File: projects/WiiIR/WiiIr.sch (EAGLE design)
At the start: 20 parts

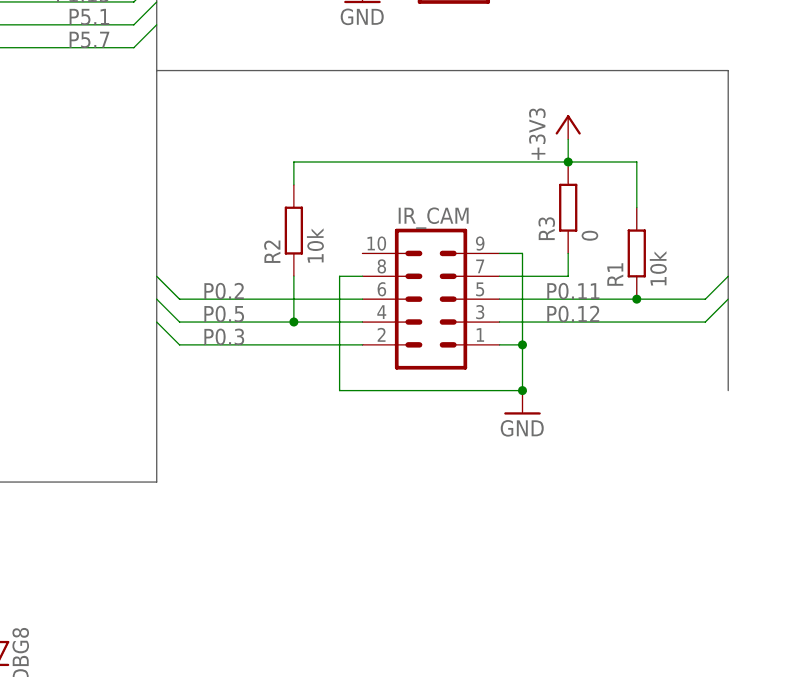
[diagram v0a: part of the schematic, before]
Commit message: Restructured + PCB v1 issues solved
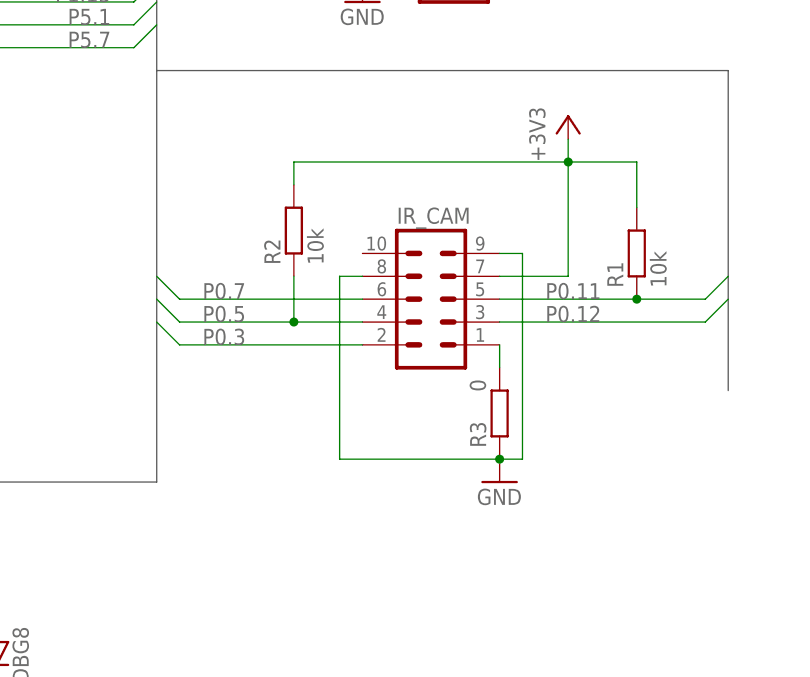
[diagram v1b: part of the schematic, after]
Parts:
- C2: device resistor:C-EU050-024X044 -> resistor:C-EU025-025X050
- R1: device resistor:R-EU_0207/10 -> resistor:R-EU_0207/15
- R3: device resistor:R-EU_0207/12 -> resistor:R-EU_0207/10
- SV1, SV2: device con-lstb:MA20-2 -> con-lstb:MA20-2BIG
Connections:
- removed net N$1: IR_CAM.7, R3.1
- new net N$12: IR_CAM.1, R3.1
- net +3V3: now also IR_CAM.7; no longer R3.2
- net GND: now also R3.2; no longer IR_CAM.1
- net P0.2: no longer IR_CAM.6
- net P0.7: now also IR_CAM.6
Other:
- moved on the sheet: R3
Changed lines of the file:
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@@
 </classes>
 <parts>
-<part name="SV1" library="con-lstb" deviceset="MA20-2" device=""/>
-<part name="SV2" library="con-lstb" deviceset="MA20-2" device=""/>
+<part name="SV1" library="con-lstb" deviceset="MA20-2" device="BIG"/>
+<part name="SV2" library="con-lstb" deviceset="MA20-2" device="BIG"/>
 <part name="GND1" library="supply1" deviceset="GND" device=""/>
 <part name="GND2" library="supply1" deviceset="GND" device=""/>
@@
 <part name="GND8" library="supply1" deviceset="GND" device=""/>
 <part name="+3V6" library="supply1" deviceset="+3V3" device=""/>
-<part name="R1" library="resistor" deviceset="R-EU_" device="0207/10" value="10k"/>
+<part name="R1" library="resistor" deviceset="R-EU_" device="0207/15" value="10k"/>
 <part name="R2" library="resistor" deviceset="R-EU_" device="0207/10" value="10k"/>
-<part name="R3" library="resistor" deviceset="R-EU_" device="0207/12" value="0"/>
 <part name="DBG_R" library="resistor-sil" deviceset="G08R" device="" value="100"/>
 <part name="DBG1" library="led" deviceset="LED" device="SQR2X5"/>
@@
 <part name="GND6" library="supply1" deviceset="GND" device=""/>
 <part name="C1" library="resistor" deviceset="CPOL-EU" device="E2.5-7" value="100u"/>
-<part name="C2" library="resistor" deviceset="C-EU" device="050-024X044" value="100n"/>
+<part name="C2" library="resistor" deviceset="C-EU" device="025-025X050" value="100n"/>
 <part name="MOTOR" library="pinhead" deviceset="PINHD-1X3" device="/90"/>
 <part name="SERVO" library="pinhead" deviceset="PINHD-1X3" device="/90"/>
+<part name="R3" library="resistor" deviceset="R-EU_" device="0207/10" value="0"/>
 </parts>
 <sheets>
@@
 <attribute name="NAME" x="34.798" y="67.31" size="1.778" layer="95" rot="R90"/>
 </instance>
-<instance part="GND5" gate="1" x="215.9" y="66.04"/>
+<instance part="GND5" gate="1" x="213.36" y="58.42"/>
 <instance part="+3V5" gate="G$1" x="220.98" y="99.06"/>
 <instance part="GND8" gate="1" x="48.26" y="58.42"/>
@@
 <instance part="R1" gate="G$1" x="228.6" y="83.82" rot="R90"/>
 <instance part="R2" gate="G$1" x="190.5" y="86.36" rot="R90"/>
-<instance part="R3" gate="G$1" x="220.98" y="88.9" rot="R90"/>
 <instance part="DBG_R" gate="G$1" x="119.38" y="22.86" rot="R180"/>
 <instance part="DBG1" gate="G$1" x="86.36" y="40.64"/>
@@
 <instance part="MOTOR" gate="A" x="210.82" y="142.24"/>
 <instance part="SERVO" gate="A" x="210.82" y="116.84"/>
+<instance part="R3" gate="G$1" x="213.36" y="66.04" smashed="yes" rot="R270">
+<attribute name="NAME" x="211.8614" y="62.23" size="1.778" layer="95" rot="R90"/>
+<attribute name="VALUE" x="210.058" y="69.85" size="1.778" layer="96" rot="R270"/>
+</instance>
 </instances>
 <busses>
@@
 <wire x1="190.5" y1="93.98" x2="220.98" y2="93.98" width="0.1524" layer="91"/>
 <junction x="220.98" y="93.98"/>
-<pinref part="R3" gate="G$1" pin="2"/>
+<pinref part="IR_CAM" gate="G$1" pin="7"/>
+<wire x1="213.36" y1="81.28" x2="220.98" y2="81.28" width="0.1524" layer="91"/>
+<wire x1="220.98" y1="81.28" x2="220.98" y2="93.98" width="0.1524" layer="91"/>
 </segment>
 <segment>
@@
 </segment>
 <segment>
-<pinref part="IR_CAM" gate="G$1" pin="9"/>
 <pinref part="GND5" gate="1" pin="GND"/>
-<wire x1="213.36" y1="83.82" x2="215.9" y2="83.82" width="0.1524" layer="91"/>
-<wire x1="215.9" y1="83.82" x2="215.9" y2="73.66" width="0.1524" layer="91"/>
-<pinref part="IR_CAM" gate="G$1" pin="1"/>
-<wire x1="215.9" y1="73.66" x2="215.9" y2="68.58" width="0.1524" layer="91"/>
-<wire x1="213.36" y1="73.66" x2="215.9" y2="73.66" width="0.1524" layer="91"/>
 <pinref part="IR_CAM" gate="G$1" pin="8"/>
 <wire x1="198.12" y1="81.28" x2="195.58" y2="81.28" width="0.1524" layer="91"/>
-<wire x1="195.58" y1="81.28" x2="195.58" y2="68.58" width="0.1524" layer="91"/>
-<wire x1="195.58" y1="68.58" x2="215.9" y2="68.58" width="0.1524" layer="91"/>
-<junction x="215.9" y="68.58"/>
-<junction x="215.9" y="73.66"/>
+<wire x1="195.58" y1="81.28" x2="195.58" y2="60.96" width="0.1524" layer="91"/>
+<wire x1="195.58" y1="60.96" x2="213.36" y2="60.96" width="0.1524" layer="91"/>
+<pinref part="R3" gate="G$1" pin="2"/>
+<junction x="213.36" y="60.96"/>
+<pinref part="IR_CAM" gate="G$1" pin="9"/>
+<wire x1="213.36" y1="83.82" x2="215.9" y2="83.82" width="0.1524" layer="91"/>
+<wire x1="215.9" y1="83.82" x2="215.9" y2="60.96" width="0.1524" layer="91"/>
+<wire x1="215.9" y1="60.96" x2="213.36" y2="60.96" width="0.1524" layer="91"/>
 </segment>
 <segment>
@@
 <wire x1="91.44" y1="132.08" x2="88.9" y2="134.62" width="0.1524" layer="91"/>
 <label x="93.98" y="132.08" size="1.778" layer="95"/>
+</segment>
+<segment>
+<pinref part="IR_CAM" gate="G$1" pin="6"/>
+<wire x1="198.12" y1="78.74" x2="177.8" y2="78.74" width="0.1524" layer="91"/>
+<wire x1="177.8" y1="78.74" x2="175.26" y2="81.28" width="0.1524" layer="91"/>
+<label x="180.34" y="78.74" size="1.778" layer="95"/>
 </segment>
 </net>
@@
 <label x="170.18" y="139.7" size="1.778" layer="95" rot="MR0"/>
 </segment>
-<segment>
-<pinref part="IR_CAM" gate="G$1" pin="6"/>
-<wire x1="198.12" y1="78.74" x2="177.8" y2="78.74" width="0.1524" layer="91"/>
-<wire x1="177.8" y1="78.74" x2="175.26" y2="81.28" width="0.1524" layer="91"/>
-<label x="180.34" y="78.74" size="1.778" layer="95"/>
-</segment>
 </net>
 <net name="P0.4" class="0">
@@
 <wire x1="172.72" y1="142.24" x2="175.26" y2="144.78" width="0.1524" layer="91"/>
 <label x="170.18" y="142.24" size="1.778" layer="95" rot="MR0"/>
-</segment>
-</net>
-<net name="N$1" class="0">
-<segment>
-<pinref part="IR_CAM" gate="G$1" pin="7"/>
-<pinref part="R3" gate="G$1" pin="1"/>
-<wire x1="213.36" y1="81.28" x2="220.98" y2="81.28" width="0.1524" layer="91"/>
-<wire x1="220.98" y1="81.28" x2="220.98" y2="83.82" width="0.1524" layer="91"/>
 </segment>
 </net>
@@
 </segment>
 </net>
+<net name="N$12" class="0">
+<segment>
+<pinref part="R3" gate="G$1" pin="1"/>
+<pinref part="IR_CAM" gate="G$1" pin="1"/>
+<wire x1="213.36" y1="73.66" x2="213.36" y2="71.12" width="0.1524" layer="91"/>
+</segment>
+</net>

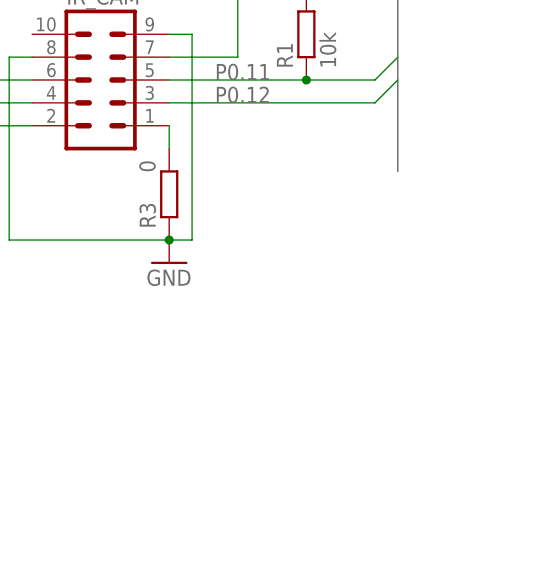
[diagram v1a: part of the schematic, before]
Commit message: IR_CAM description, optimizations
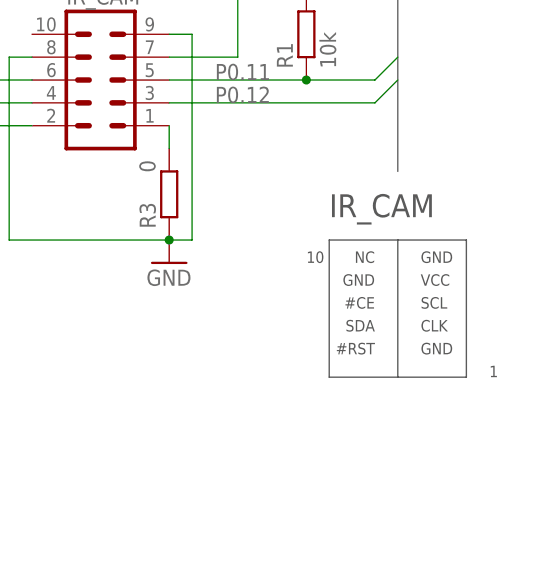
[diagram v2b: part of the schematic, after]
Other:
- note added: "#CE"
- note added: "#RST"
- note added: "1"
- note added: "10"
- note added: "CLK"
- note added: "GND"
- note added: "IR_CAM"
- note added: "NC"
- note added: "SCL"
- note added: "SDA"
- note added: "VCC"
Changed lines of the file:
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@@
 <grid distance="0.1" unitdist="inch" unit="inch" style="lines" multiple="1" display="no" altdistance="0.01" altunitdist="inch" altunit="inch"/>
 <layers>
-<layer number="1" name="Top" color="4" fill="1" visible="yes" active="no"/>
-<layer number="16" name="Bottom" color="1" fill="1" visible="yes" active="no"/>
-<layer number="17" name="Pads" color="2" fill="1" visible="yes" active="no"/>
-<layer number="18" name="Vias" color="2" fill="1" visible="yes" active="no"/>
-<layer number="19" name="Unrouted" color="6" fill="1" visible="yes" active="no"/>
-<layer number="20" name="Dimension" color="15" fill="1" visible="yes" active="no"/>
-<layer number="21" name="tPlace" color="7" fill="1" visible="yes" active="no"/>
-<layer number="22" name="bPlace" color="7" fill="1" visible="yes" active="no"/>
-<layer number="23" name="tOrigins" color="15" fill="1" visible="yes" active="no"/>
-<layer number="24" name="bOrigins" color="15" fill="1" visible="yes" active="no"/>
-<layer number="25" name="tNames" color="7" fill="1" visible="yes" active="no"/>
-<layer number="26" name="bNames" color="7" fill="1" visible="yes" active="no"/>
-<layer number="27" name="tValues" color="7" fill="1" visible="yes" active="no"/>
-<layer number="28" name="bValues" color="7" fill="1" visible="yes" active="no"/>
+<layer number="1" name="Top" color="4" fill="1" visible="no" active="no"/>
+<layer number="16" name="Bottom" color="1" fill="1" visible="no" active="no"/>
+<layer number="17" name="Pads" color="2" fill="1" visible="no" active="no"/>
+<layer number="18" name="Vias" color="2" fill="1" visible="no" active="no"/>
+<layer number="19" name="Unrouted" color="6" fill="1" visible="no" active="no"/>
+<layer number="20" name="Dimension" color="15" fill="1" visible="no" active="no"/>
+<layer number="21" name="tPlace" color="7" fill="1" visible="no" active="no"/>
+<layer number="22" name="bPlace" color="7" fill="1" visible="no" active="no"/>
+<layer number="23" name="tOrigins" color="15" fill="1" visible="no" active="no"/>
+<layer number="24" name="bOrigins" color="15" fill="1" visible="no" active="no"/>
+<layer number="25" name="tNames" color="7" fill="1" visible="no" active="no"/>
+<layer number="26" name="bNames" color="7" fill="1" visible="no" active="no"/>
+<layer number="27" name="tValues" color="7" fill="1" visible="no" active="no"/>
+<layer number="28" name="bValues" color="7" fill="1" visible="no" active="no"/>
 <layer number="29" name="tStop" color="7" fill="3" visible="no" active="no"/>
 <layer number="30" name="bStop" color="7" fill="6" visible="no" active="no"/>
@@
 <layer number="35" name="tGlue" color="7" fill="4" visible="no" active="no"/>
 <layer number="36" name="bGlue" color="7" fill="5" visible="no" active="no"/>
-<layer number="37" name="tTest" color="7" fill="1" visible="yes" active="no"/>
-<layer number="38" name="bTest" color="7" fill="1" visible="yes" active="no"/>
+<layer number="37" name="tTest" color="7" fill="1" visible="no" active="no"/>
+<layer number="38" name="bTest" color="7" fill="1" visible="no" active="no"/>
 <layer number="39" name="tKeepout" color="4" fill="11" visible="no" active="no"/>
 <layer number="40" name="bKeepout" color="1" fill="11" visible="no" active="no"/>
@@
 <layer number="44" name="Drills" color="7" fill="1" visible="no" active="no"/>
 <layer number="45" name="Holes" color="7" fill="1" visible="no" active="no"/>
-<layer number="46" name="Milling" color="3" fill="1" visible="yes" active="no"/>
-<layer number="47" name="Measures" color="7" fill="1" visible="yes" active="no"/>
-<layer number="48" name="Document" color="7" fill="1" visible="yes" active="no"/>
-<layer number="49" name="Reference" color="7" fill="1" visible="yes" active="no"/>
-<layer number="51" name="tDocu" color="7" fill="1" visible="yes" active="no"/>
-<layer number="52" name="bDocu" color="7" fill="1" visible="yes" active="no"/>
+<layer number="46" name="Milling" color="3" fill="1" visible="no" active="no"/>
+<layer number="47" name="Measures" color="7" fill="1" visible="no" active="no"/>
+<layer number="48" name="Document" color="7" fill="1" visible="no" active="no"/>
+<layer number="49" name="Reference" color="7" fill="1" visible="no" active="no"/>
+<layer number="51" name="tDocu" color="7" fill="1" visible="no" active="no"/>
+<layer number="52" name="bDocu" color="7" fill="1" visible="no" active="no"/>
 <layer number="91" name="Nets" color="2" fill="1" visible="yes" active="yes"/>
 <layer number="92" name="Busses" color="1" fill="1" visible="yes" active="yes"/>
@@
 <sheet>
 <plain>
+<text x="236.22" y="58.42" size="1.27" layer="97" rot="MR0">NC</text>
+<text x="241.3" y="58.42" size="1.27" layer="97">GND</text>
+<text x="236.22" y="55.88" size="1.27" layer="97" rot="MR0">GND</text>
+<text x="241.3" y="48.26" size="1.27" layer="97">GND</text>
+<text x="241.3" y="55.88" size="1.27" layer="97">VCC</text>
+<text x="241.3" y="53.34" size="1.27" layer="97">SCL</text>
+<text x="236.22" y="53.34" size="1.27" layer="97" rot="MR0">#CE</text>
+<text x="241.3" y="50.8" size="1.27" layer="97">CLK</text>
+<text x="236.22" y="50.8" size="1.27" layer="97" rot="MR0">SDA</text>
+<text x="236.22" y="48.26" size="1.27" layer="97" rot="MR0">#RST</text>
+<wire x1="238.76" y1="60.96" x2="231.14" y2="60.96" width="0.1524" layer="97"/>
+<wire x1="231.14" y1="60.96" x2="231.14" y2="45.72" width="0.1524" layer="97"/>
+<wire x1="231.14" y1="45.72" x2="238.76" y2="45.72" width="0.1524" layer="97"/>
+<wire x1="238.76" y1="45.72" x2="246.38" y2="45.72" width="0.1524" layer="97"/>
+<wire x1="246.38" y1="45.72" x2="246.38" y2="60.96" width="0.1524" layer="97"/>
+<wire x1="246.38" y1="60.96" x2="238.76" y2="60.96" width="0.1524" layer="97"/>
+<wire x1="238.76" y1="60.96" x2="238.76" y2="45.72" width="0.1524" layer="97"/>
+<text x="248.92" y="45.72" size="1.27" layer="97">1</text>
+<text x="228.6" y="58.42" size="1.27" layer="97">10</text>
+<text x="231.14" y="63.5" size="2.54" layer="97">IR_CAM</text>
 </plain>
 <instances>
